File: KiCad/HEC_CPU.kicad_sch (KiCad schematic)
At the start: 23 parts, among them J3 Conn_02x05_Odd_Even, J9 Conn_02x14_Odd_Even, SW2 SW_Push, U1 Z80CPU, U10 74LS32, U20 74LS574, U21 74LS574, U22 74LS02, U30 74LS74, U34 74LS393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

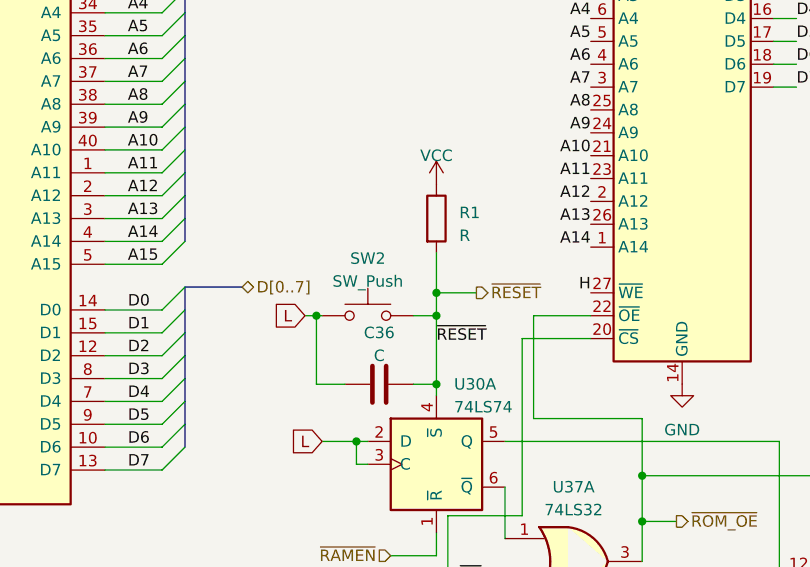
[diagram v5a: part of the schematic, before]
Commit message: change NX bit to XE bit
change No eXecute to eXecute Enable (inverting the polarity of the signal) in order to fix a bug that causes the HEC to not recognize a NX when the instruction fetched is a RST.
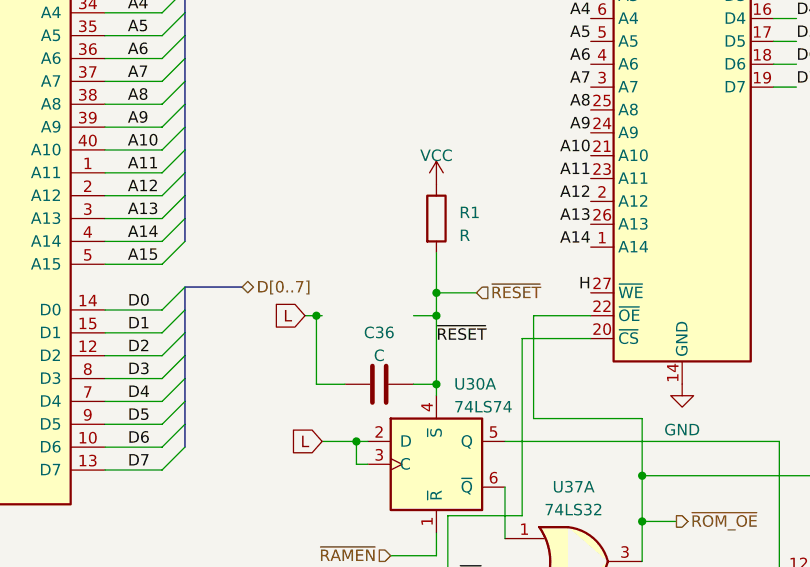
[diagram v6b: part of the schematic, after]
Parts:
- removed SW2: SW_Push, Button_Switch_THT:SW_PUSH_6mm, symbol Switch:SW_Push
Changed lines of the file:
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@@
     )
   )
-  (hierarchical_label "~{RESET}" (shape output) (at 106.045 65.405 0) (fields_autoplaced)
+  (hierarchical_label "~{RESET}" (shape input) (at 106.045 65.405 0) (fields_autoplaced)
     (effects (font (size 1.27 1.27)) (justify left))
   )
@@
         )
       )
-    )
-  )
-  (symbol (lib_id "Switch:SW_Push") (at 93.98 67.945 0) (mirror y) (unit 1)
-    (in_bom yes) (on_board yes) (dnp no) (fields_autoplaced)
-    (property "Reference" "SW2" (at 93.98 61.595 0)
-      (effects (font (size 1.27 1.27)))
-    )
-    (property "Value" "SW_Push" (at 93.98 64.135 0)
-      (effects (font (size 1.27 1.27)))
-    )
-    (property "Footprint" "Button_Switch_THT:SW_PUSH_6mm" (at 93.98 62.865 0)
-      (effects (font (size 1.27 1.27)) hide)
-    )
-    (property "Datasheet" "~" (at 93.98 62.865 0)
-      (effects (font (size 1.27 1.27)) hide)
-    )
-    (pin "1")
-    (pin "2")
-    (instances
-      (project "HEC1"
-        (path "/87935374-b60a-4f41-99da-94b76103dd77/73a0c68b-1e42-4c0d-ae31-b1a96d0648bb"
-          (reference "SW2") (unit 1)
-        )
-      )

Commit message: Fixed reversed POST code display
Wrote a program to test the POST code LED display, found out it's backwards, and fixed it in schematic
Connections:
- net at U38.1 (B): now also U36.19 (Q0); no longer U36.14 (Q5)
- net at U38.2 (C): now also U36.18 (Q1); no longer U36.13 (Q6)
- net at U38.6 (D): now also U36.16 (Q3); no longer U36.12 (Q7)
- net at U38.7 (A): now also U36.17 (Q2); no longer U36.15 (Q4)
- net at U39.6 (D): now also U36.12 (Q7); no longer U36.16 (Q3)
- net at U39.7 (A): now also U36.15 (Q4); no longer U36.17 (Q2)
- net at U39.2 (C): now also U36.13 (Q6); no longer U36.18 (Q1)
- net at U39.1 (B): now also U36.14 (Q5); no longer U36.19 (Q0)
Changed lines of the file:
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@@
+    (stroke (width 0) (type default))
+  )
+  (wire (pts (xy 184.15 57.15) (xy 184.15 33.02))
     (stroke (width 0) (type default))
   )
@@
     (stroke (width 0) (type default))
   )
+  (wire (pts (xy 182.245 25.4) (xy 182.245 49.53))
+    (stroke (width 0) (type default))
+  )
   (wire (pts (xy 198.12 92.71) (xy 198.12 114.935))
     (stroke (width 0) (type default))
@@
     (stroke (width 0) (type default))
   )
-  (wire (pts (xy 181.61 77.47) (xy 192.405 77.47))
-    (stroke (width 0) (type default))
-  )
   (wire (pts (xy 235.585 33.02) (xy 239.395 33.02))
     (stroke (width 0) (type default))
   )
-  (wire (pts (xy 181.61 27.94) (xy 192.405 27.94))
-    (stroke (width 0) (type default))
-  )
   (wire (pts (xy 157.48 160.02) (xy 157.48 170.18))
     (stroke (width 0) (type default))
   )
+  (wire (pts (xy 182.245 49.53) (xy 181.61 49.53))
+    (stroke (width 0) (type default))
+  )
   (wire (pts (xy 97.79 140.97) (xy 97.79 160.02))
     (stroke (width 0) (type default))
@@
     (stroke (width 0) (type default))
   )
+  (wire (pts (xy 186.69 72.39) (xy 192.405 72.39))
+    (stroke (width 0) (type default))
+  )
   (wire (pts (xy 201.93 148.59) (xy 215.9 148.59))
     (stroke (width 0) (type default))
@@
     (stroke (width 0) (type default))
   )
+  (wire (pts (xy 182.88 52.07) (xy 182.88 27.94))
+    (stroke (width 0) (type default))
+  )
   (wire (pts (xy 64.77 59.69) (xy 71.12 59.69))
     (stroke (width 0) (type default))
@@
     (stroke (width 0) (type default))
   )
-  (wire (pts (xy 181.61 57.15) (xy 181.61 77.47))
-    (stroke (width 0) (type default))
-  )
   (wire (pts (xy 239.395 40.64) (xy 239.395 38.1))
     (stroke (width 0) (type default))
   )
+  (wire (pts (xy 185.42 46.99) (xy 185.42 77.47))
+    (stroke (width 0) (type default))
+  )
   (wire (pts (xy 238.76 35.56) (xy 235.585 35.56))
     (stroke (width 0) (type default))
@@
     (stroke (width 0) (type default))
   )
+  (wire (pts (xy 187.96 44.45) (xy 187.96 69.85))
+    (stroke (width 0) (type default))
+  )
   (wire (pts (xy 64.77 80.01) (xy 71.12 80.01))
     (stroke (width 0) (type default))
@@
     (stroke (width 0) (type default))
   )
-  (wire (pts (xy 185.42 25.4) (xy 185.42 44.45))
-    (stroke (width 0) (type default))
-  )
   (wire (pts (xy 26.67 57.15) (xy 29.21 57.15))
     (stroke (width 0) (type default))
@@
     (stroke (width 0) (type default))
   )
+  (wire (pts (xy 186.055 41.91) (xy 186.055 74.93))
+    (stroke (width 0) (type default))
+  )
   (wire (pts (xy 227.965 78.74) (xy 227.965 80.01))
     (stroke (width 0) (type default))
@@
     (stroke (width 0) (type default))
   )
-  (wire (pts (xy 181.61 44.45) (xy 185.42 44.45))
+  (wire (pts (xy 181.61 44.45) (xy 187.96 44.45))
     (stroke (width 0) (type default))
   )
@@
     (stroke (width 0) (type default))
   )
+  (wire (pts (xy 181.61 54.61) (xy 183.515 54.61))
+    (stroke (width 0) (type default))
+  )
   (wire (pts (xy 133.35 140.97) (xy 133.35 160.02))
     (stroke (width 0) (type default))
@@
     (stroke (width 0) (type default))
   )
-  (wire (pts (xy 181.61 52.07) (xy 185.42 52.07))
+  (wire (pts (xy 181.61 52.07) (xy 182.88 52.07))
     (stroke (width 0) (type default))
   )
@@
     (stroke (width 0) (type default))
   )
-  (wire (pts (xy 192.405 74.93) (xy 183.515 74.93))
+  (wire (pts (xy 181.61 39.37) (xy 186.69 39.37))
+    (stroke (width 0) (type default))
+  )
+  (wire (pts (xy 192.405 74.93) (xy 186.055 74.93))
     (stroke (width 0) (type default))
   )
@@
     (stroke (width 0) (type default))
   )
-  (wire (pts (xy 183.515 74.93) (xy 183.515 54.61))
+  (wire (pts (xy 181.61 57.15) (xy 184.15 57.15))
     (stroke (width 0) (type default))
   )
@@
     (stroke (width 0) (type default))
   )
-  (wire (pts (xy 187.325 46.99) (xy 187.325 33.02))
-    (stroke (width 0) (type default))
-  )
   (wire (pts (xy 274.955 38.1) (xy 282.575 38.1))
     (stroke (width 0) (type default))
@@
     (stroke (width 0) (type default))
   )
+  (wire (pts (xy 184.15 33.02) (xy 192.405 33.02))
+    (stroke (width 0) (type default))
+  )
   (wire (pts (xy 109.22 97.79) (xy 109.22 101.6))
     (stroke (width 0) (type default))
@@
     (stroke (width 0) (type default))
   )
-  (wire (pts (xy 183.515 54.61) (xy 181.61 54.61))
+  (wire (pts (xy 185.42 77.47) (xy 192.405 77.47))
     (stroke (width 0) (type default))
   )
@@
     (stroke (width 0) (type default))
   )
-  (wire (pts (xy 187.325 69.85) (xy 187.325 49.53))
-    (stroke (width 0) (type default))
-  )
   (wire (pts (xy 64.77 69.85) (xy 71.12 69.85))
     (stroke (width 0) (type default))
@@
     (stroke (width 0) (type default))
   )
-  (wire (pts (xy 181.61 41.91) (xy 183.515 41.91))
+  (wire (pts (xy 181.61 41.91) (xy 186.055 41.91))
     (stroke (width 0) (type default))
   )
@@
     (stroke (width 0) (type default))
   )
+  (wire (pts (xy 182.88 27.94) (xy 192.405 27.94))
+    (stroke (width 0) (type default))
+  )
   (wire (pts (xy 20.32 74.93) (xy 29.21 74.93))
     (stroke (width 0) (type default))
@@
     (stroke (width 0) (type default))
   )
+  (wire (pts (xy 183.515 54.61) (xy 183.515 30.48))
+    (stroke (width 0) (type default))
+  )
   (wire (pts (xy 242.57 45.72) (xy 242.57 53.34))
     (stroke (width 0) (type default))
@@
     (stroke (width 0) (type default))
   )
+  (wire (pts (xy 186.69 39.37) (xy 186.69 72.39))
+    (stroke (width 0) (type default))
+  )
   (wire (pts (xy 99.06 75.565) (xy 101.6 75.565))
     (stroke (width 0) (type default))
@@
     (stroke (width 0) (type default))
   )
-  (wire (pts (xy 192.405 69.85) (xy 187.325 69.85))
+  (wire (pts (xy 192.405 69.85) (xy 187.96 69.85))
     (stroke (width 0) (type default))
   )
@@
     (stroke (width 0) (type default))
   )
-  (wire (pts (xy 187.325 49.53) (xy 181.61 49.53))
-    (stroke (width 0) (type default))
-  )
   (wire (pts (xy 222.885 33.02) (xy 225.425 33.02))
     (stroke (width 0) (type default))
@@
     (stroke (width 0) (type default))
   )
-  (wire (pts (xy 192.405 25.4) (xy 185.42 25.4))
-    (stroke (width 0) (type default))
-  )
-  (wire (pts (xy 185.42 52.07) (xy 185.42 72.39))
+  (wire (pts (xy 192.405 25.4) (xy 182.245 25.4))
     (stroke (width 0) (type default))
   )
@@
     (stroke (width 0) (type default))
   )
-  (wire (pts (xy 183.515 41.91) (xy 183.515 30.48))
-    (stroke (width 0) (type default))
-  )
   (wire (pts (xy 91.44 138.43) (xy 93.98 138.43))
     (stroke (width 0) (type default))
@@
     (stroke (width 0) (type default))
   )
-  (wire (pts (xy 185.42 72.39) (xy 192.405 72.39))
-    (stroke (width 0) (type default))
-  )
-  (wire (pts (xy 181.61 27.94) (xy 181.61 39.37))
-    (stroke (width 0) (type default))
-  )
   (wire (pts (xy 279.4 80.01) (xy 258.445 80.01))
     (stroke (width 0) (type default))
@@
     (stroke (width 0) (type default))
   )
-  (wire (pts (xy 181.61 46.99) (xy 187.325 46.99))
-    (stroke (width 0) (type default))
-  )
-  (wire (pts (xy 187.325 33.02) (xy 192.405 33.02))
-    (stroke (width 0) (type default))
-  )
+  (wire (pts (xy 181.61 46.99) (xy 185.42 46.99))
+    (stroke (width 0) (type default))
+  )

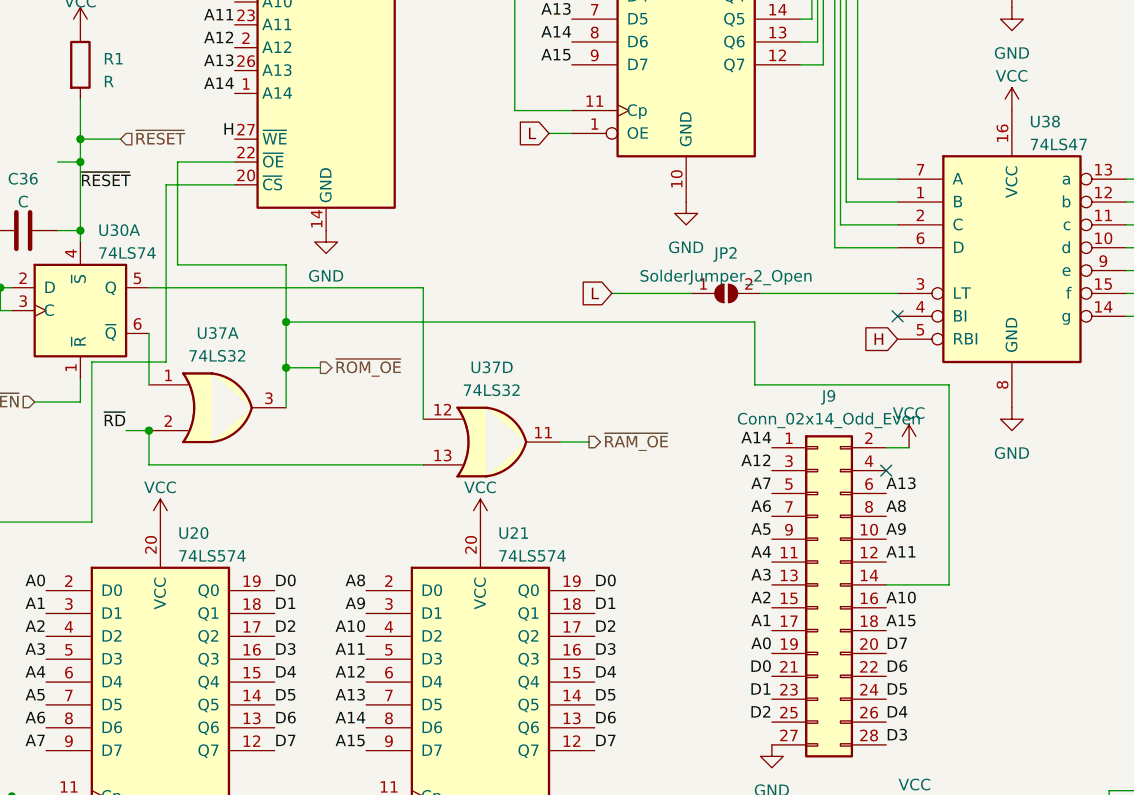
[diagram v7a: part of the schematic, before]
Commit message: VERA bringup
Brought up VERA, streamlines firmware build process.
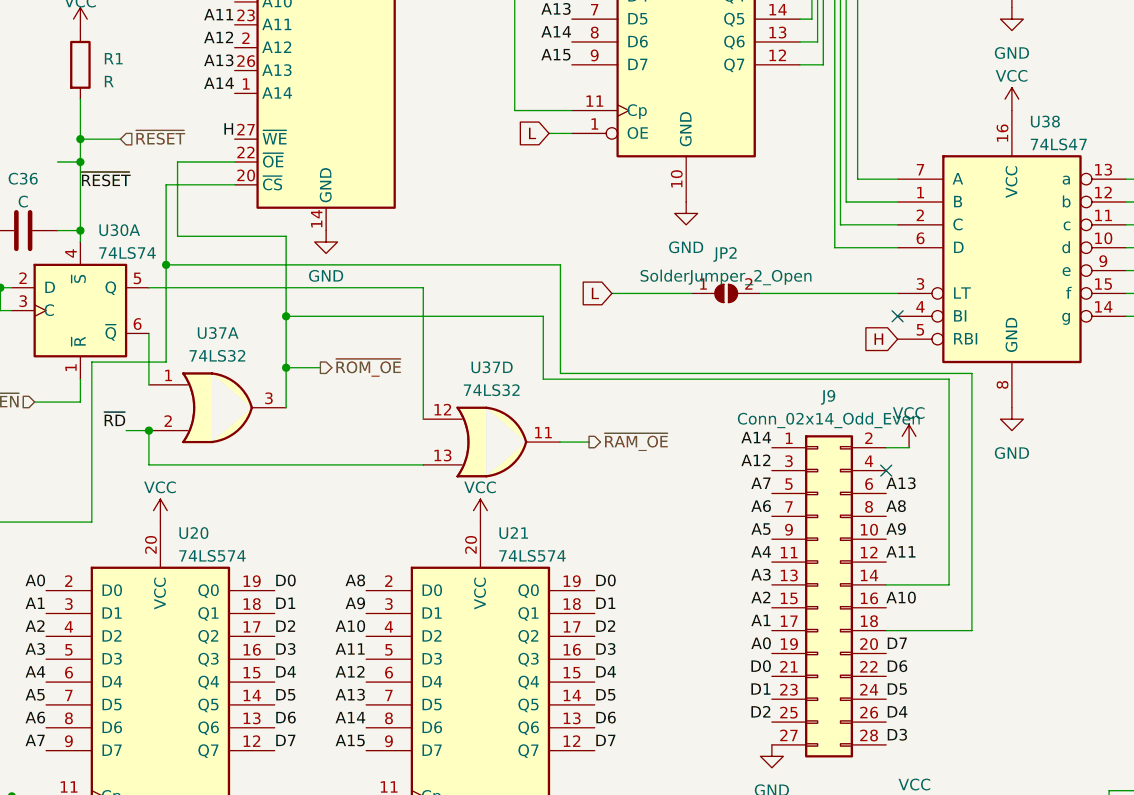
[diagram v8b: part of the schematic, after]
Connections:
- net A15: no longer J9.18 (Pin_18)
- net at U37.8, U7.20 (~{CS}): now also J9.18 (Pin_18)
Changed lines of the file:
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@@
   (junction (at 92.71 81.915) (diameter 0) (color 0 0 0 0)
   )
-  (junction (at 124.46 85.725) (diameter 0) (color 0 0 0 0)
-  )
   (junction (at 245.11 137.795) (diameter 0) (color 0 0 0 0)
   )
   (junction (at 88.265 67.945) (diameter 0) (color 0 0 0 0)
   )
+  (junction (at 111.125 79.375) (diameter 0) (color 0 0 0 0)
+  )
   (junction (at 105.41 172.72) (diameter 0) (color 0 0 0 0)
   )
   (junction (at 109.22 97.79) (diameter 0) (color 0 0 0 0)
+  )
+  (junction (at 124.46 85.09) (diameter 0) (color 0 0 0 0)
   )
   (junction (at 93.98 138.43) (diameter 0) (color 0 0 0 0)
@@
     (stroke (width 0) (type default))
   )
-  (wire (pts (xy 198.12 92.71) (xy 198.12 114.935))
+  (wire (pts (xy 198.12 92.075) (xy 198.12 114.935))
     (stroke (width 0) (type default))
   )
@@
     (stroke (width 0) (type default))
   )
+  (wire (pts (xy 200.66 120.015) (xy 191.135 120.015))
+    (stroke (width 0) (type default))
+  )
   (wire (pts (xy 240.03 31.75) (xy 240.03 33.02))
     (stroke (width 0) (type default))
@@
     (stroke (width 0) (type default))
   )
-  (wire (pts (xy 111.125 70.485) (xy 111.125 90.17))
+  (wire (pts (xy 111.125 70.485) (xy 111.125 79.375))
     (stroke (width 0) (type default))
   )
@@
     (stroke (width 0) (type default))
   )
-  (wire (pts (xy 176.53 85.725) (xy 176.53 92.71))
+  (wire (pts (xy 153.035 85.09) (xy 153.035 92.075))
     (stroke (width 0) (type default))
   )
@@
     (stroke (width 0) (type default))
   )
-  (wire (pts (xy 124.46 85.725) (xy 176.53 85.725))
+  (wire (pts (xy 200.66 91.44) (xy 200.66 120.015))
+    (stroke (width 0) (type default))
+  )
+  (wire (pts (xy 124.46 85.09) (xy 153.035 85.09))
     (stroke (width 0) (type default))
   )
@@
     (stroke (width 0) (type default))
   )
+  (wire (pts (xy 154.94 79.375) (xy 154.94 91.44))
+    (stroke (width 0) (type default))
+  )
   (wire (pts (xy 235.585 40.64) (xy 238.125 40.64))
     (stroke (width 0) (type default))
@@
     (stroke (width 0) (type default))
   )
-  (wire (pts (xy 176.53 92.71) (xy 198.12 92.71))
+  (wire (pts (xy 153.035 92.075) (xy 198.12 92.075))
     (stroke (width 0) (type default))
   )
@@
     (stroke (width 0) (type default))
   )
-  (wire (pts (xy 112.395 67.945) (xy 112.395 79.375))
+  (wire (pts (xy 112.395 67.945) (xy 112.395 76.2))
     (stroke (width 0) (type default))
   )
@@
     (stroke (width 0) (type default))
   )
-  (wire (pts (xy 124.46 85.725) (xy 124.46 90.805))
-    (stroke (width 0) (type default))
-  )
   (wire (pts (xy 222.885 31.75) (xy 222.885 33.02))
     (stroke (width 0) (type default))
@@
     (stroke (width 0) (type default))
   )
+  (wire (pts (xy 111.125 79.375) (xy 154.94 79.375))
+    (stroke (width 0) (type default))
+  )
   (wire (pts (xy 224.155 69.85) (xy 224.155 78.74))
     (stroke (width 0) (type default))
@@
     (stroke (width 0) (type default))
   )
-  (wire (pts (xy 112.395 79.375) (xy 124.46 79.375))
+  (wire (pts (xy 112.395 76.2) (xy 124.46 76.2))
     (stroke (width 0) (type default))
   )
@@
     (stroke (width 0) (type default))
   )
+  (wire (pts (xy 154.94 91.44) (xy 200.66 91.44))
+    (stroke (width 0) (type default))
+  )
   (wire (pts (xy 242.57 45.72) (xy 244.475 45.72))
     (stroke (width 0) (type default))
@@
     (stroke (width 0) (type default))
   )
+  (wire (pts (xy 111.125 79.375) (xy 111.125 90.17))
+    (stroke (width 0) (type default))
+  )
   (wire (pts (xy 221.615 39.37) (xy 224.79 39.37))
     (stroke (width 0) (type default))
@@
     (stroke (width 0) (type default))
   )
-  (wire (pts (xy 124.46 79.375) (xy 124.46 85.725))
+  (wire (pts (xy 124.46 76.2) (xy 124.46 85.09))
     (stroke (width 0) (type default))
   )
@@
   )
   (wire (pts (xy 64.77 74.93) (xy 71.12 74.93))
+    (stroke (width 0) (type default))
+  )
+  (wire (pts (xy 124.46 85.09) (xy 124.46 90.805))
     (stroke (width 0) (type default))
   )
@@
     (effects (font (size 1.27 1.27)) (justify right bottom))
   )
-  (label "A15" (at 191.135 120.015 0) (fields_autoplaced)
-    (effects (font (size 1.27 1.27)) (justify left bottom))
-  )
   (label "A11" (at 191.135 112.395 0) (fields_autoplaced)
